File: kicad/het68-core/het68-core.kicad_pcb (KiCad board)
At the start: 6 copper layers, 160 x 100 mm, 134 parts, among them J1 MIC1, J11 PZ1, J12 PZ2, J13 PZ3, J14 PZ4, J2 MIC2, J3 MIC3, J4 MIC4, J5 MIC5, J6 MIC6, U1 RP2350B, U10 SN65LVDS047, U11 SN65LVDS047, U12 SN65LVDS047, U13 SN65LVDS32, U14 SN65LVDS32, U2 W25Q128JVSIQ, U3 APS6404L, U4 AP2112K-3.3, U5 AP2112K-1.8, U6 DRV8837C, U7 DPS310, U8 SHT40, U9 ADXL355, Y1 12MHz

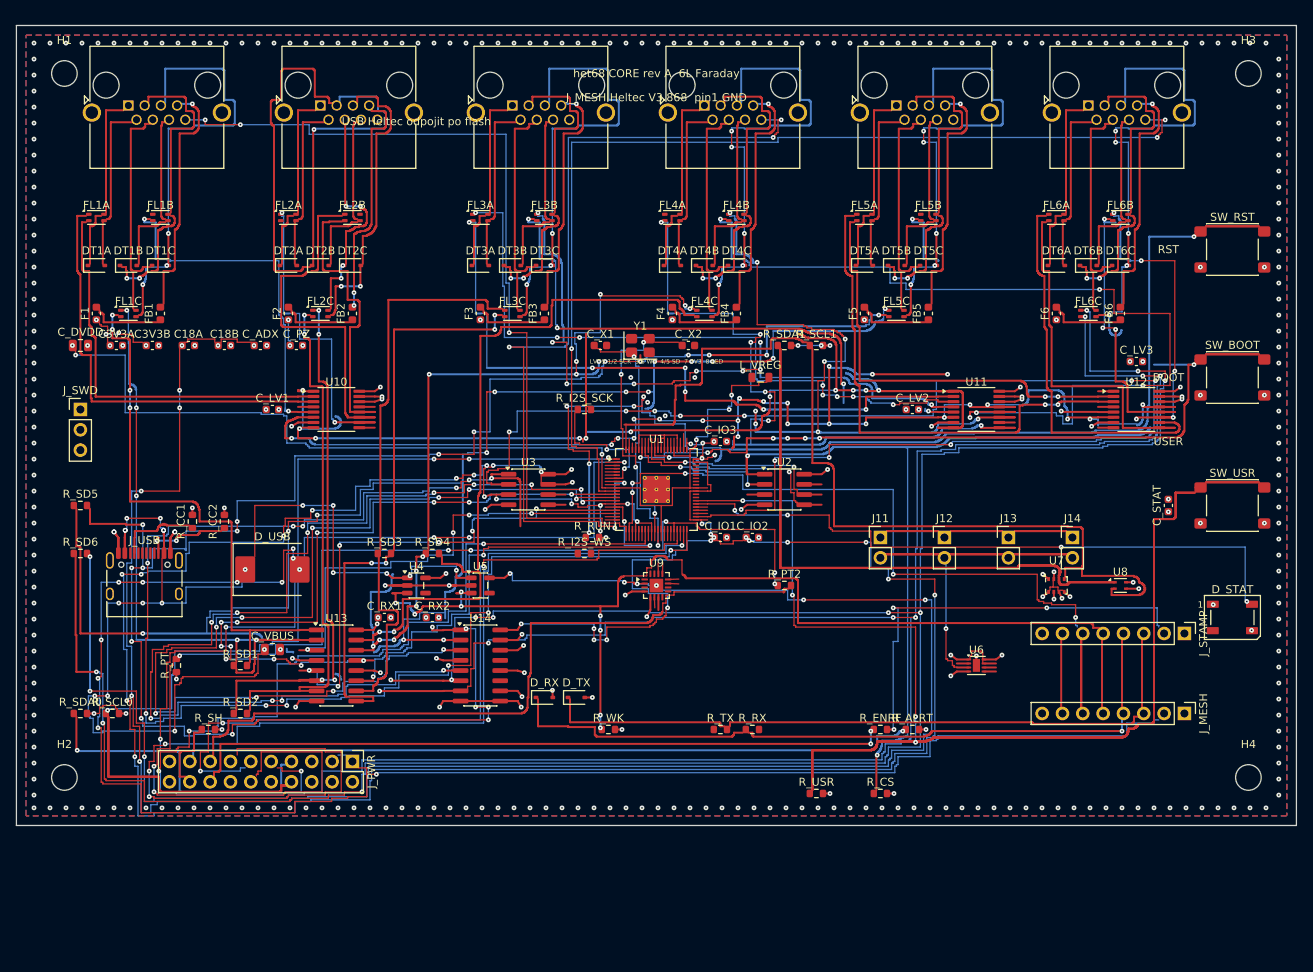
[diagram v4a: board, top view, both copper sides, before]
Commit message: Put the satellite electronics on the back and clear the power-board pad shorts.
The outward face keeps only the microphone hole and the eight SK6812s. The DO-201 and the two regulators move off the header so the power boards no longer short pad to pad. Some LVDS, QSPI and GPIO nets are still open.

Co-authored-by: Cursor <cursoragent@cursor.com>
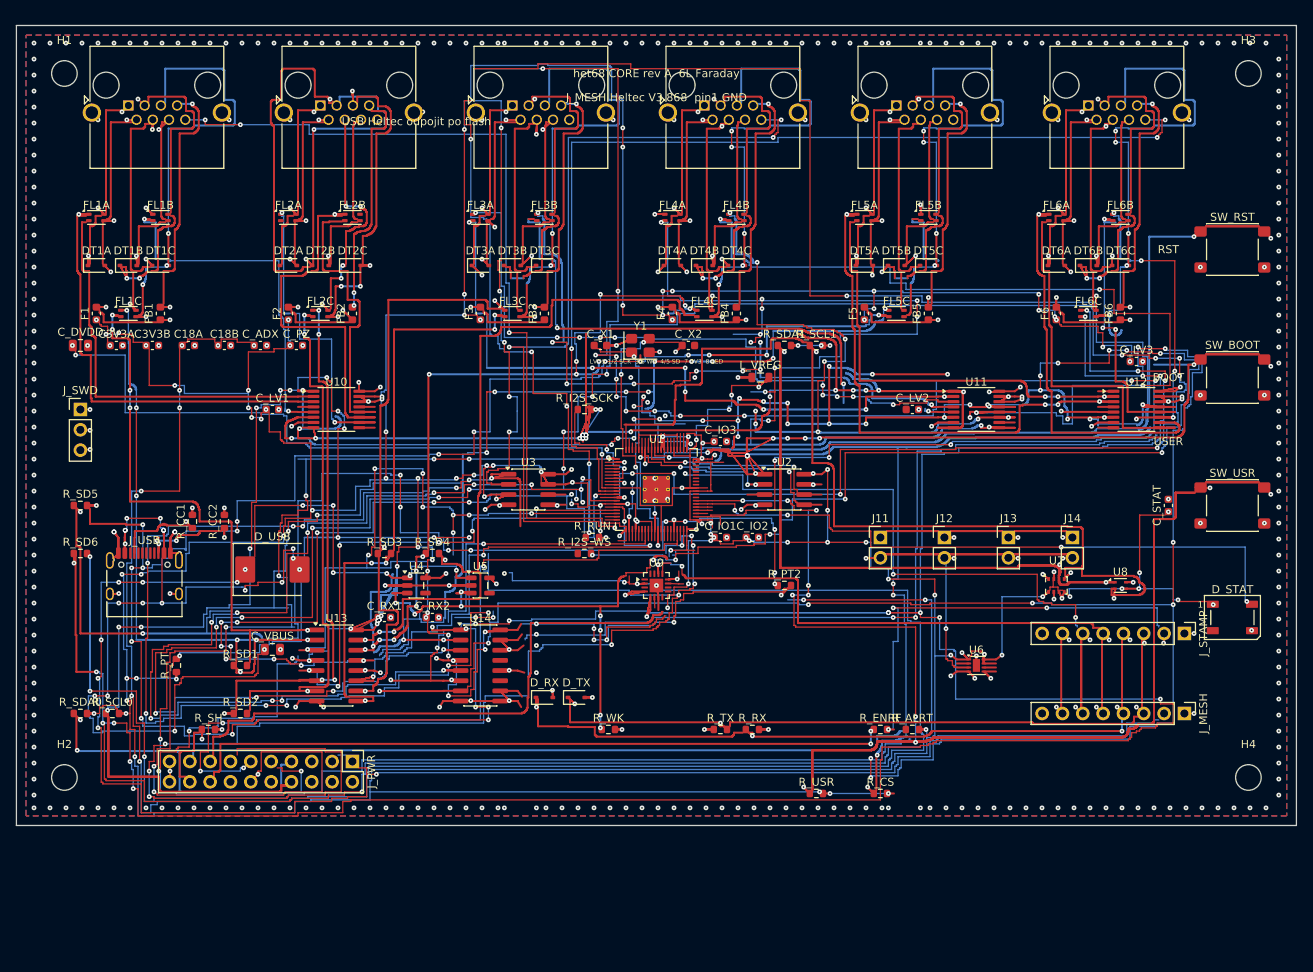
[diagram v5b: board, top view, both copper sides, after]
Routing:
- net +3V3_DIG: track 474.7 -> 1193.4 mm, vias 86 -> 140
- net GND: track 105.7 -> 580.9 mm, vias 314 -> 351
- net SD6_P: track 317.1 -> 557.1 mm, vias 12 -> 22
- net I2S_SD5: track 133.2 -> 351.5 mm, vias 10 -> 23
- net RUN: track 152.2 -> 336.2 mm, vias 6 -> 10
- net I2S_WS: track 181.1 -> 343.4 mm, vias 24 -> 37
- net PSRAM_SO: track 175.0 -> 280.0 mm, vias 10 -> 20
- net I2S_SCK: track 172.8 -> 277.6 mm, vias 11 -> 20
- net QSPI_SS: track 213.1 -> 307.3 mm, vias 9 -> 16
- net SD6_N: track 310.4 -> 380.4 mm, vias 10 -> 16
- net SCK4_N: track 88.9 -> 147.6 mm, vias 6 -> 12
- net VBUS: track 106.2 -> 156.3 mm, vias 17 -> 19
- net PT1000_RTN: track 93.9 -> 139.5 mm, vias 0 -> 6
- net +1V8_AUDIO: track 262.2 -> 306.9 mm
- net I2C0_SCL: track 164.5 -> 208.8 mm, vias 4 -> 14
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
